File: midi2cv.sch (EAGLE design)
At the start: 21 parts, among them IC1 LM324N

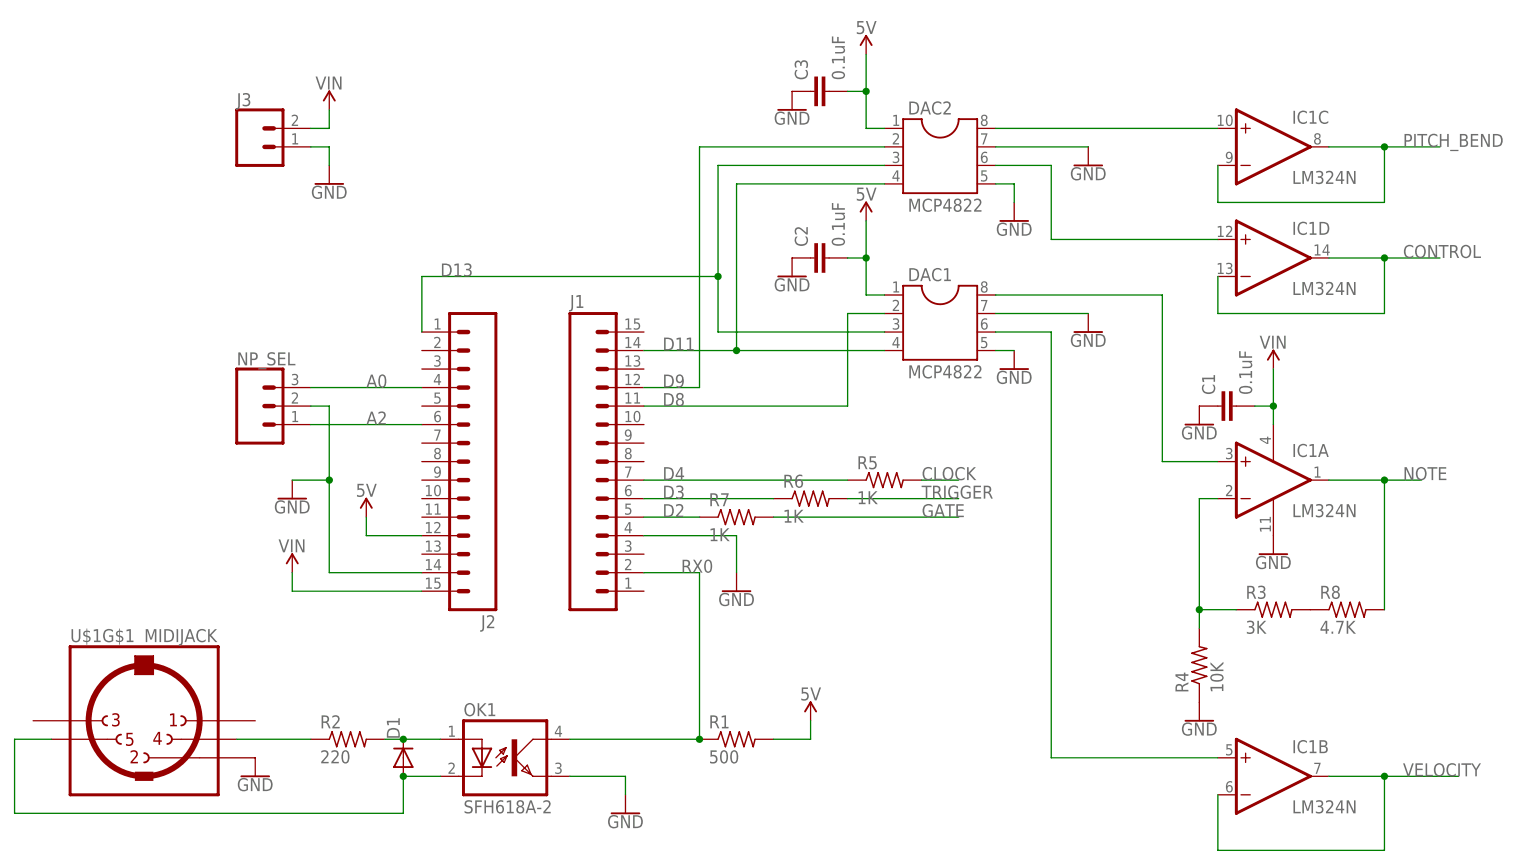
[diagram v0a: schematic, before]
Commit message: adapted project for triggering drum modules
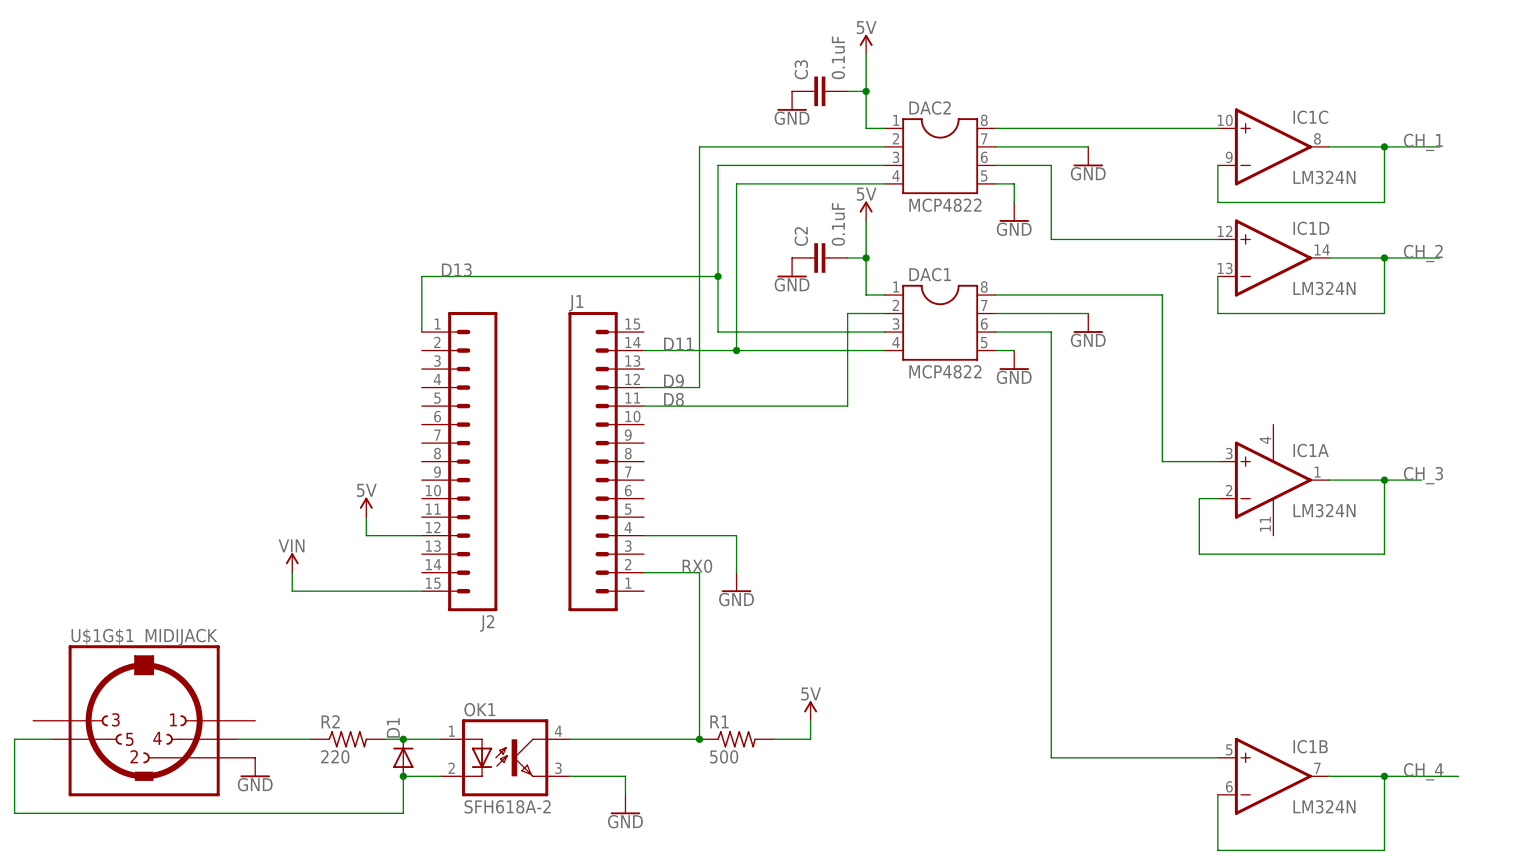
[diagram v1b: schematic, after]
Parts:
- removed C1: 0.1uF, SparkFun-Capacitors:0.1UF-KIT-EZ-50V-20%
- removed J3: (no value), SparkFun-Connectors:CONN_025MM
- removed NP_SEL: (no value), SparkFun-Connectors:CONN_03
- removed R3: 3K, resistor:R-US_0207/10
- removed R4: 10K, resistor:R-US_0207/10
- removed R5, R6, R7: 1K, resistor:R-US_0207/10
- removed R8: 4.7K, resistor:R-US_0207/10
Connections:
- net CONTROL renamed CH_2
- net PITCH_BEND renamed CH_1
- net VELOCITY renamed CH_4
- removed net A0: J2.4, NP_SEL.3
- removed net A2: J2.6, NP_SEL.1
- removed net CLOCK: R5.2
- removed net D2: J1.5, R7.1
- removed net D3: J1.6, R6.1
- removed net D4: J1.7, R5.1
- removed net GATE: R7.2
- removed net N$5: R3.2, R8.1
- removed net N$6: IC1A.-IN, R3.1, R4.2
- removed net NOTE: IC1A.OUT, R8.2
- removed net TRIGGER: R6.2
- new net CH_3: IC1A.-IN, IC1A.OUT
- net GND: no longer C1.1, IC1P.V-, J2.14, J3.1, NP_SEL.2, R4.1
- net VIN: no longer C1.2, IC1P.V+, J3.2
